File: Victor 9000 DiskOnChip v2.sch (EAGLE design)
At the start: 9 parts

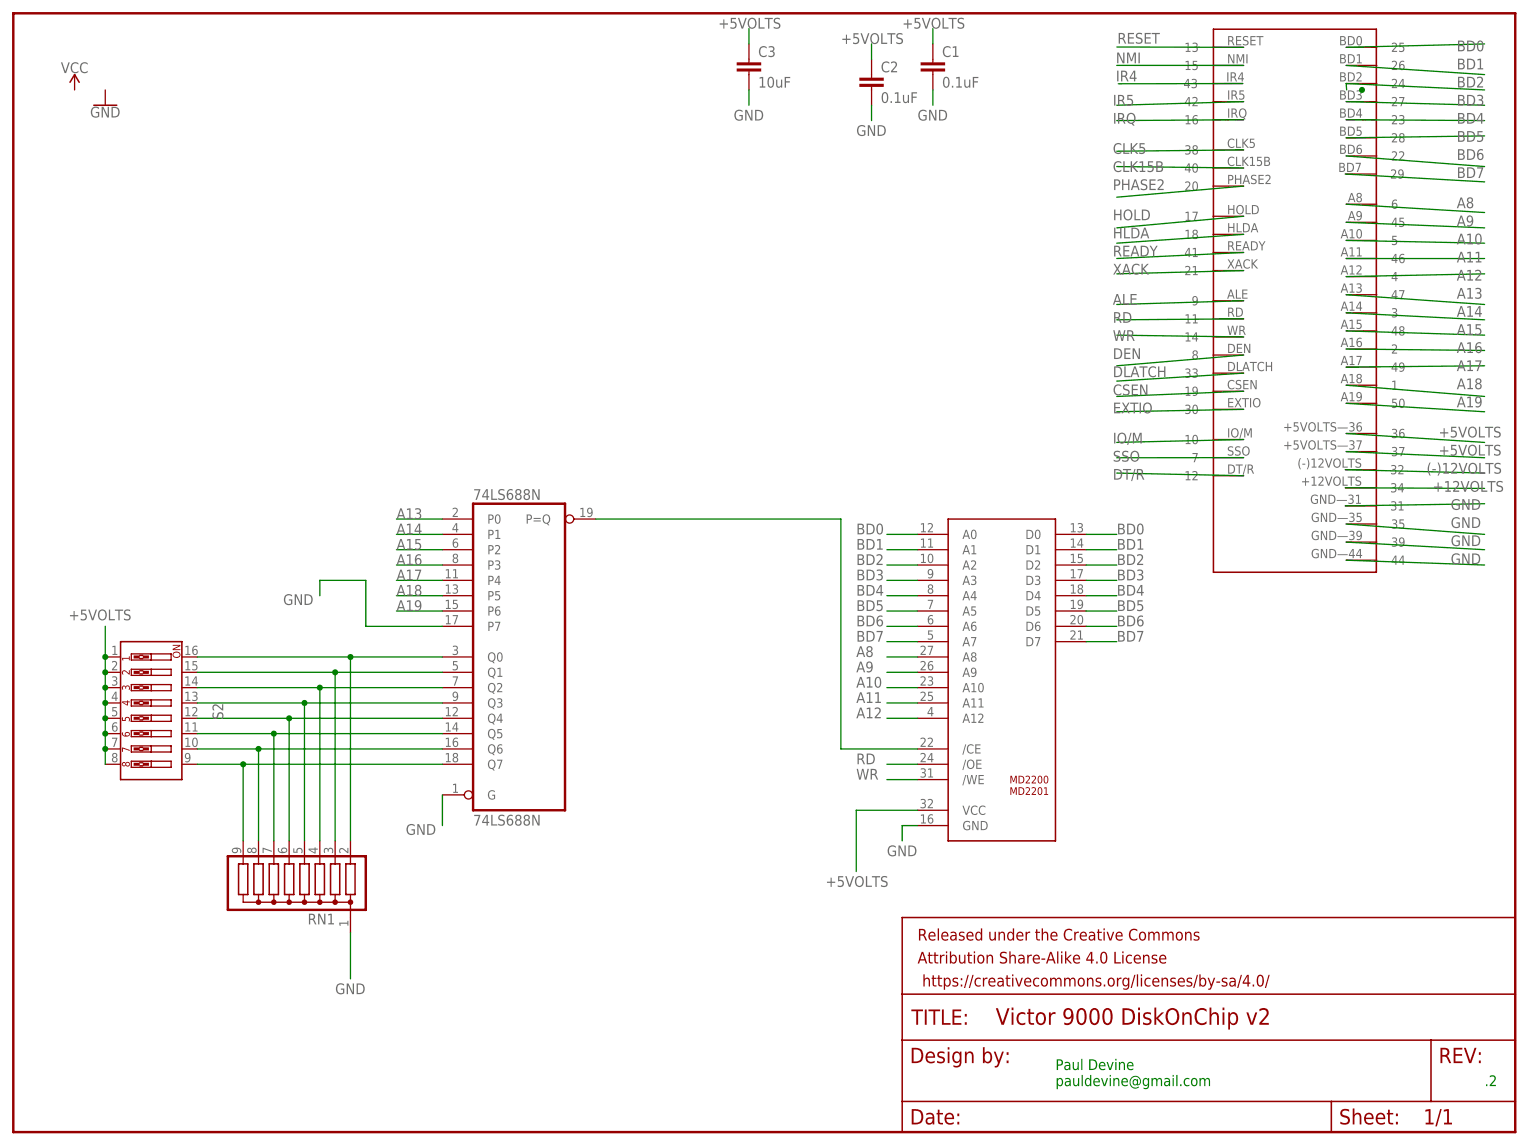
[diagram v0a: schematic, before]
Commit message: cleaned up schematic
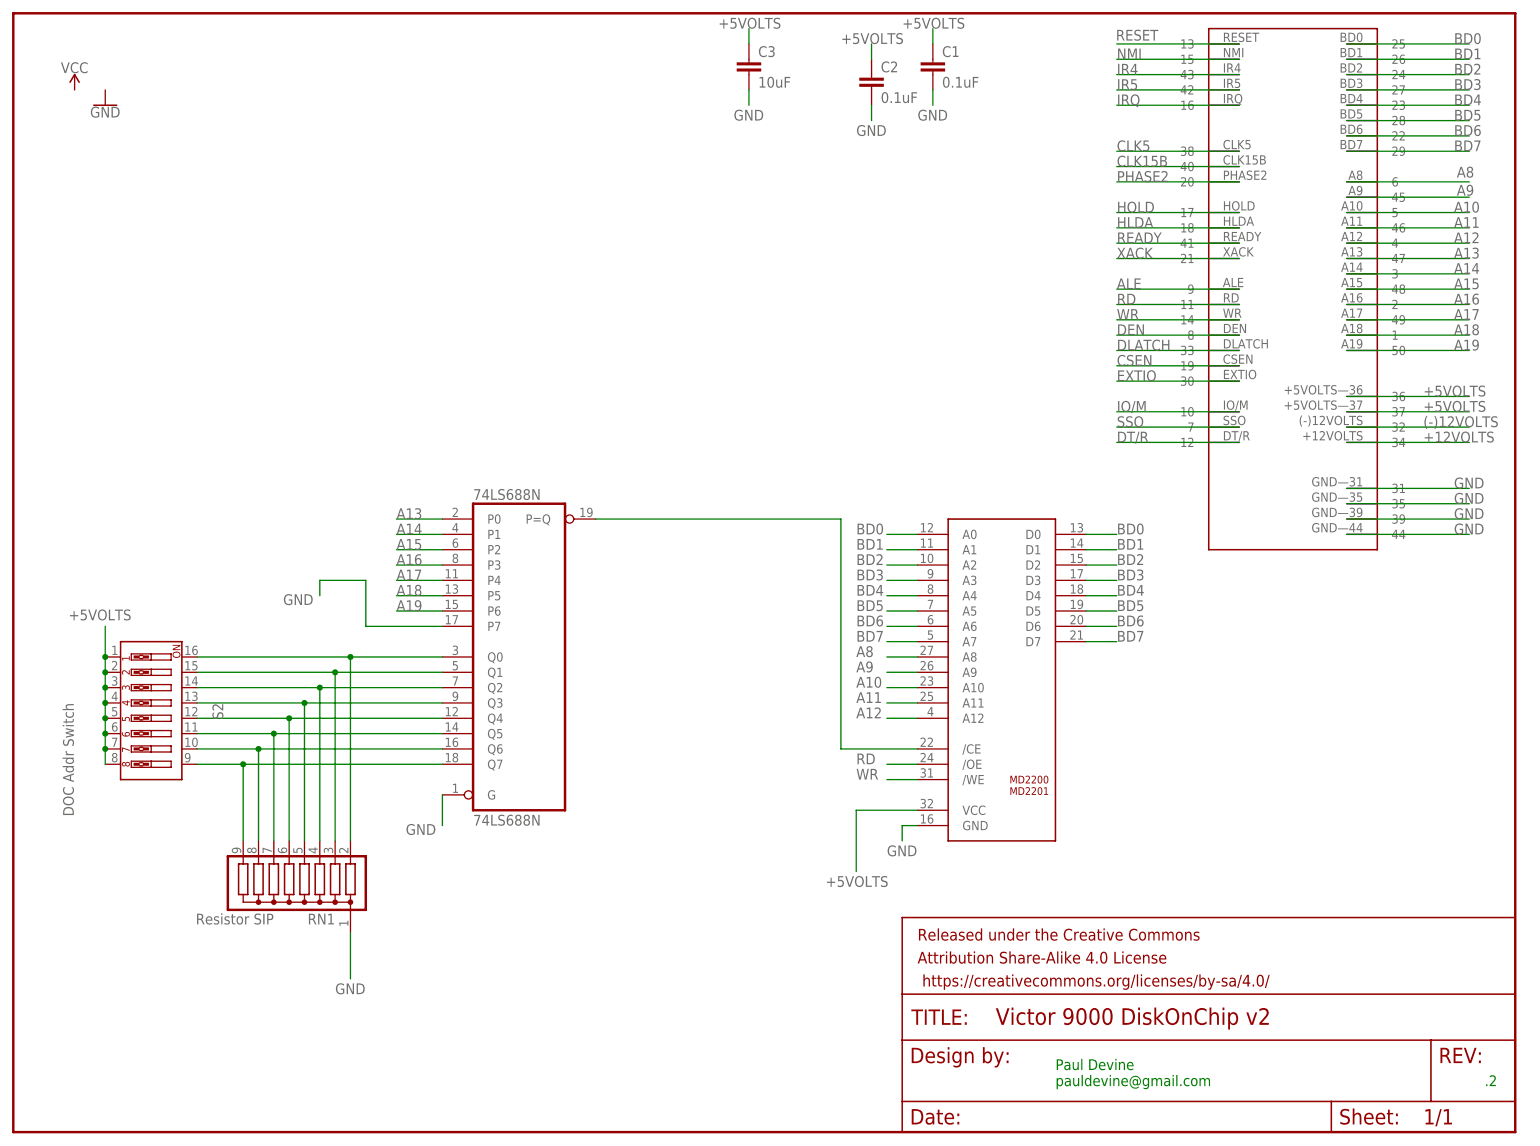
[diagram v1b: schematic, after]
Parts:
- RN1: value (none) -> Resistor SIP
- S2: value (none) -> DOC Addr Switch

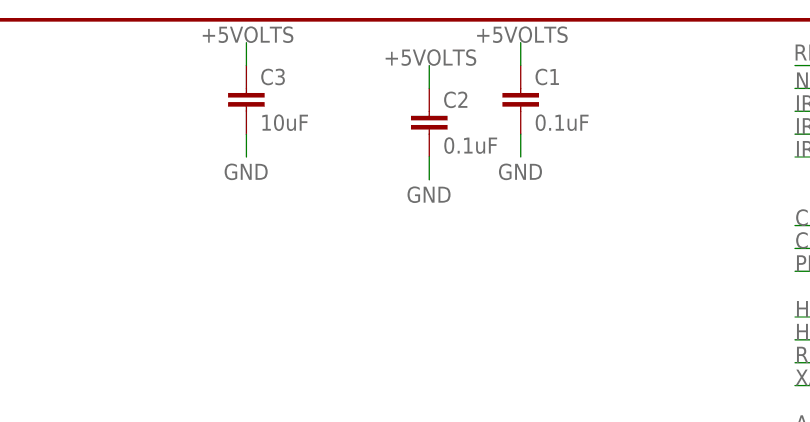
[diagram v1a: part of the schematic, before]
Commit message: fixed capacitors to be through hole rather than SMD
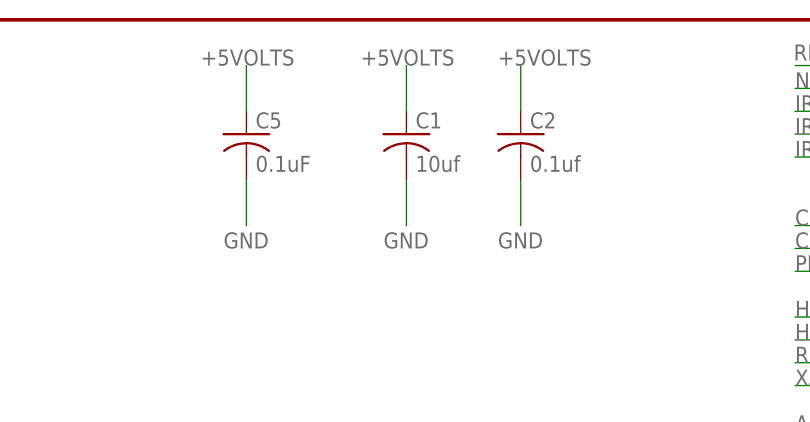
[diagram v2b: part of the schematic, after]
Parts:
- removed C3: 10uF, SparkFun-Capacitors:10UF-1210-50V-20%
- added C5: 0.1uF, rcl:C-US025-050X050
- C1: value 0.1uF -> 10uf; device SparkFun-Capacitors:0.1UF-0603-25V-5% -> rcl:C-US025-050X050
- C2: value 0.1uF -> 0.1uf; device SparkFun-Capacitors:0.1UF-0603-25V-5% -> rcl:C-US025-050X050
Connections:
- net +5VOLTS: now also C5.1; no longer C3.1
- net GND: now also C5.2; no longer C3.2
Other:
- moved on the sheet: C1, C2
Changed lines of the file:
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@@
 <setting verticaltext="up"/>
 </settings>
-<grid distance="0.1" unitdist="inch" unit="mm" style="lines" multiple="1" display="yes" altdistance="0.01" altunitdist="inch" altunit="inch"/>
+<grid distance="0.1" unitdist="inch" unit="mm" style="lines" multiple="1" display="no" altdistance="0.01" altunitdist="inch" altunit="inch"/>
 <layers>
 <layer number="1" name="Top" color="4" fill="1" visible="no" active="no"/>
@@
 <part name="GND1" library="SparkFun-PowerSymbols" library_urn="urn:adsk.eagle:library:530" deviceset="GND" device=""/>
 <part name="U$1" library="pauldevine_library" deviceset="VICTOR_GOLD_FINGERS" device=""/>
-<part name="C1" library="SparkFun-Capacitors" library_urn="urn:adsk.eagle:library:510" deviceset="0.1UF" device="-0603-25V-5%" package3d_urn="urn:adsk.eagle:package:37414/1" value="0.1uF"/>
-<part name="C2" library="SparkFun-Capacitors" library_urn="urn:adsk.eagle:library:510" deviceset="0.1UF" device="-0603-25V-5%" package3d_urn="urn:adsk.eagle:package:37414/1" value="0.1uF"/>
-<part name="C3" library="SparkFun-Capacitors" library_urn="urn:adsk.eagle:library:510" deviceset="10UF" device="-1210-50V-20%" package3d_urn="urn:adsk.eagle:package:37436/1" value="10uF"/>
 <part name="RN1" library="resistor-sil" library_urn="urn:adsk.eagle:library:347" deviceset="G08R" device="" package3d_urn="urn:adsk.eagle:package:25282/1" value="Resistor SIP"/>
+<part name="C5" library="rcl" library_urn="urn:adsk.eagle:library:334" deviceset="C-US" device="025-050X050" package3d_urn="urn:adsk.eagle:package:23633/1" value="0.1uF"/>
+<part name="C1" library="rcl" library_urn="urn:adsk.eagle:library:334" deviceset="C-US" device="025-050X050" package3d_urn="urn:adsk.eagle:package:23633/1" value="10uf"/>
+<part name="C2" library="rcl" library_urn="urn:adsk.eagle:library:334" deviceset="C-US" device="025-050X050" package3d_urn="urn:adsk.eagle:package:23633/1" value="0.1uf"/>
 </parts>
 <sheets>
@@
 </instance>
 <instance part="U$1" gate="G$1" x="106.68" y="73.66" smashed="yes"/>
-<instance part="C1" gate="G$1" x="43.18" y="104.14" smashed="yes">
-<attribute name="NAME" x="44.704" y="107.061" size="1.778" layer="95" font="vector"/>
-<attribute name="VALUE" x="44.704" y="101.981" size="1.778" layer="96" font="vector"/>
-</instance>
-<instance part="C2" gate="G$1" x="33.02" y="101.6" smashed="yes">
-<attribute name="NAME" x="34.544" y="104.521" size="1.778" layer="95" font="vector"/>
-<attribute name="VALUE" x="34.544" y="99.441" size="1.778" layer="96" font="vector"/>
-</instance>
-<instance part="C3" gate="G$1" x="12.7" y="104.14" smashed="yes">
-<attribute name="NAME" x="14.224" y="107.061" size="1.778" layer="95" font="vector"/>
-<attribute name="VALUE" x="14.224" y="101.981" size="1.778" layer="96" font="vector"/>
-</instance>
 <instance part="RN1" gate="G$1" x="-63.5" y="-27.94" smashed="yes" rot="R180">
 <attribute name="NAME" x="-55.88" y="-34.925" size="1.778" layer="95" rot="R180"/>
 <attribute name="VALUE" x="-66.04" y="-34.925" size="1.778" layer="96" rot="R180"/>
+</instance>
+<instance part="C5" gate="G$1" x="12.7" y="101.6" smashed="yes">
+<attribute name="NAME" x="13.716" y="102.235" size="1.778" layer="95"/>
+<attribute name="VALUE" x="13.716" y="97.409" size="1.778" layer="96"/>
+</instance>
+<instance part="C1" gate="G$1" x="30.48" y="101.6" smashed="yes">
+<attribute name="NAME" x="31.496" y="102.235" size="1.778" layer="95"/>
+<attribute name="VALUE" x="31.496" y="97.409" size="1.778" layer="96"/>
+</instance>
+<instance part="C2" gate="G$1" x="43.18" y="101.6" smashed="yes">
+<attribute name="NAME" x="44.196" y="102.235" size="1.778" layer="95"/>
+<attribute name="VALUE" x="44.196" y="97.409" size="1.778" layer="96"/>
 </instance>
 </instances>
@@
 </segment>
 <segment>
-<pinref part="C3" gate="G$1" pin="1"/>
-<wire x1="12.7" y1="109.22" x2="12.7" y2="111.76" width="0.1524" layer="91"/>
-<label x="7.62" y="111.76" size="1.778" layer="95"/>
+<pinref part="C5" gate="G$1" pin="1"/>
+<wire x1="12.7" y1="104.14" x2="12.7" y2="109.22" width="0.1524" layer="91"/>
+<label x="7.62" y="109.22" size="1.778" layer="95"/>
+</segment>
+<segment>
+<pinref part="C1" gate="G$1" pin="1"/>
+<wire x1="30.48" y1="104.14" x2="30.48" y2="109.22" width="0.1524" layer="91"/>
+<label x="25.4" y="109.22" size="1.778" layer="95"/>
 </segment>
 <segment>
 <pinref part="C2" gate="G$1" pin="1"/>
-<wire x1="33.02" y1="106.68" x2="33.02" y2="109.22" width="0.1524" layer="91"/>
-<label x="27.94" y="109.22" size="1.778" layer="95"/>
-</segment>
-<segment>
-<pinref part="C1" gate="G$1" pin="1"/>
-<wire x1="43.18" y1="109.22" x2="43.18" y2="111.76" width="0.1524" layer="91"/>
-<label x="38.1" y="111.76" size="1.778" layer="95"/>
+<wire x1="43.18" y1="104.14" x2="43.18" y2="109.22" width="0.1524" layer="91"/>
+<label x="40.64" y="109.22" size="1.778" layer="95"/>
 </segment>
 </net>
@@
 </segment>
 <segment>
-<pinref part="C3" gate="G$1" pin="2"/>
-<wire x1="12.7" y1="101.6" x2="12.7" y2="99.06" width="0.1524" layer="91"/>
-<label x="10.16" y="96.52" size="1.778" layer="95"/>
+<pinref part="C5" gate="G$1" pin="2"/>
+<wire x1="12.7" y1="96.52" x2="12.7" y2="91.44" width="0.1524" layer="91"/>
+<label x="10.16" y="88.9" size="1.778" layer="95"/>
 </segment>
 <segment>
 <pinref part="C1" gate="G$1" pin="2"/>
-<wire x1="43.18" y1="101.6" x2="43.18" y2="99.06" width="0.1524" layer="91"/>
-<label x="40.64" y="96.52" size="1.778" layer="95"/>
+<wire x1="30.48" y1="96.52" x2="30.48" y2="91.44" width="0.1524" layer="91"/>
+<label x="27.94" y="88.9" size="1.778" layer="95"/>
 </segment>
 <segment>
 <pinref part="C2" gate="G$1" pin="2"/>
-<wire x1="33.02" y1="99.06" x2="33.02" y2="96.52" width="0.1524" layer="91"/>
-<label x="30.48" y="93.98" size="1.778" layer="95"/>
+<wire x1="43.18" y1="96.52" x2="43.18" y2="91.44" width="0.1524" layer="91"/>
+<label x="40.64" y="88.9" size="1.778" layer="95"/>
 </segment>
 </net>
@@
 packages will not be understood (or retained) with this version.
 </note>
+<note version="8.4" severity="warning">
+Since Version 8.4, EAGLE supports properties for SPICE simulation.
+Probes in schematics and SPICE mapping objects found in parts and library devices
+will not be understood with this version. Update EAGLE to the latest version
+for full support of SPICE simulation.
+</note>
 </compatibility>
